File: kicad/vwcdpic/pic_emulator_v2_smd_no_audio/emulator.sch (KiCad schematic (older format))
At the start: 11 parts, among them P1 CONN_01X05, P2 CONN_01X02, U1 PIC12F629, U2 78L05

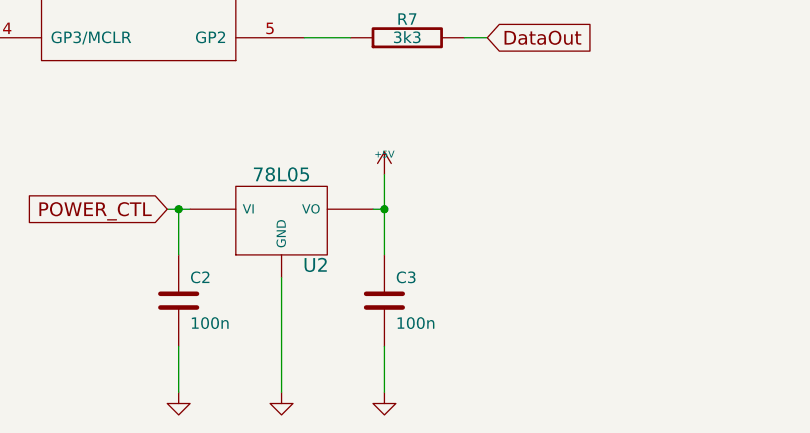
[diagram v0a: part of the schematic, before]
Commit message: update pcb with soic8 handsoldering module
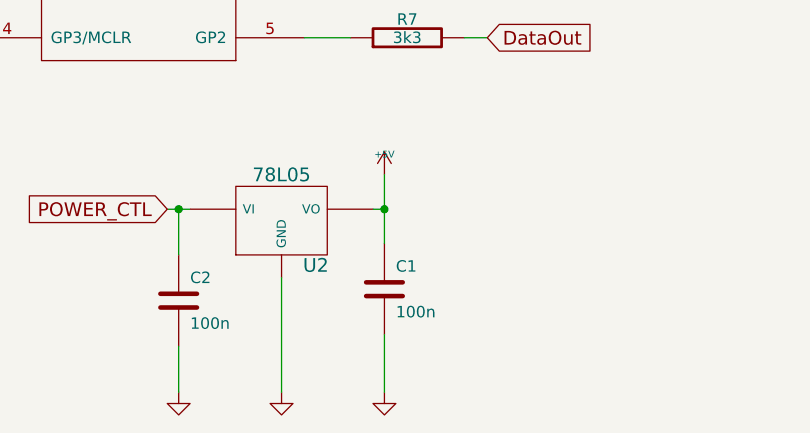
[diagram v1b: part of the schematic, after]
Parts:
- removed C3: 100n, symbol C
- added C1: 100n, symbol C
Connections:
- net +5V: now also C1.1
- net GND: now also C1.2
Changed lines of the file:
@@
 Wire Wire Line
 	5050 5050 5100 5050
-Connection ~ 5100 5050
 Wire Wire Line
 	8050 4000 8850 4000
@@
 	2200 4000 2300 4000
 Wire Wire Line
-	5100 5650 5100 5850
-Wire Wire Line
 	4200 5650 4200 5850
 Wire Wire Line
@@
 Wire Wire Line
 	4650 5350 4650 5850
-Wire Wire Line
-	5100 5250 5100 4900
 Wire Wire Line
 	4200 2850 4750 2850
@@
 $EndComp
 $Comp
-L GND #PWR07
-U 1 1 52D02F9D
-P 5100 5850
-F 0 "#PWR07" H 5100 5850 30  0001 C CNN
-F 1 "GND" H 5100 5780 30  0001 C CNN
-F 2 "" H 5100 5850 60  0001 C CNN
-F 3 "" H 5100 5850 60  0001 C CNN
-	1    5100 5850
-	1    0    0    -1
-$EndComp
-$Comp
-L C C3
-U 1 1 52D02F45
-P 5100 5450
-F 0 "C3" H 5150 5550 50  0000 L CNN
-F 1 "100n" H 5150 5350 50  0000 L CNN
-F 2 "" H 5100 5450 60  0001 C CNN
-F 3 "" H 5100 5450 60  0001 C CNN
-	1    5100 5450
-	1    0    0    -1
-$EndComp
-$Comp
 L C C2
 U 1 1 52D02F40
@@
 Wire Wire Line
 	4750 3800 4750 4000
+Wire Wire Line
+	5100 4900 5100 5200
+$Comp
+L C C1
+U 1 1 54325C4C
+P 5100 5400
+F 0 "C1" H 5150 5500 50  0000 L CNN
+F 1 "100n" H 5150 5300 50  0000 L CNN
+F 2 "" H 5100 5400 60  0001 C CNN
+F 3 "" H 5100 5400 60  0001 C CNN
+	1    5100 5400
+	1    0    0    -1
+$EndComp
+$Comp
+L GND #PWR07
+U 1 1 54325C93
+P 5100 5850
+F 0 "#PWR07" H 5100 5850 30  0001 C CNN
+F 1 "GND" H 5100 5780 30  0001 C CNN
+F 2 "" H 5100 5850 60  0001 C CNN
+F 3 "" H 5100 5850 60  0001 C CNN
+	1    5100 5850
+	1    0    0    -1
+$EndComp
+Wire Wire Line
+	5100 5600 5100 5850
+Connection ~ 5100 5050
 $EndSCHEMATC

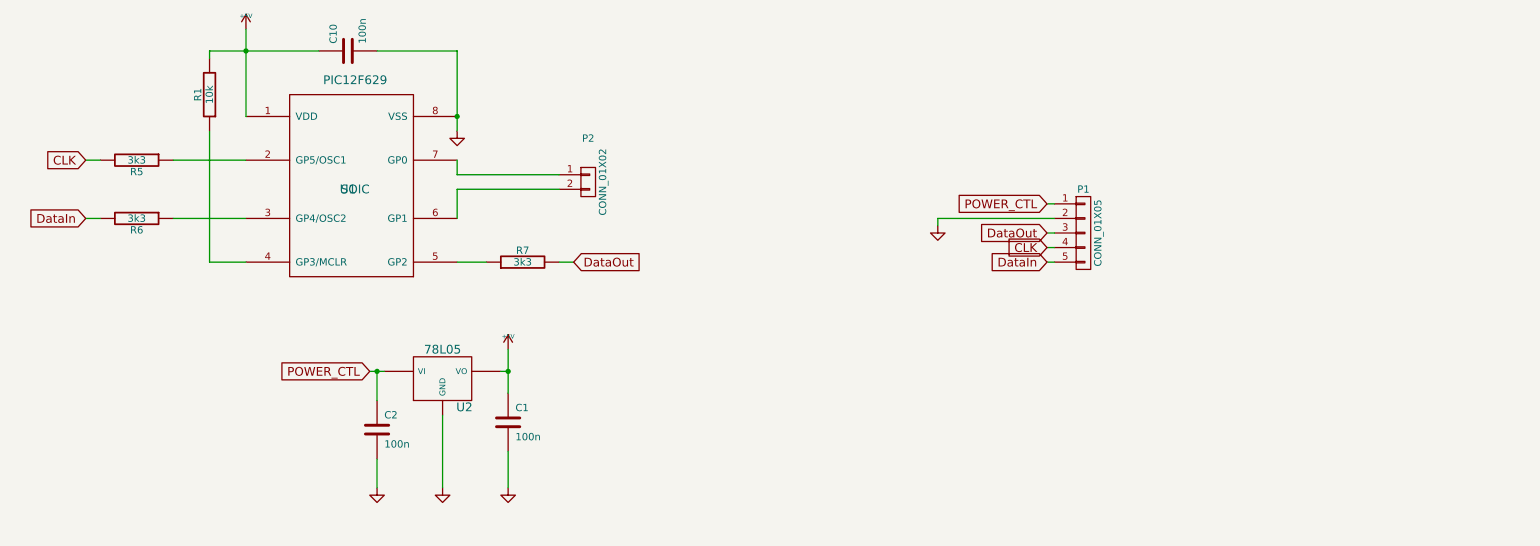
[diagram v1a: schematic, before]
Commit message: smd boards update: singleside smd, doubleside smd, minimized
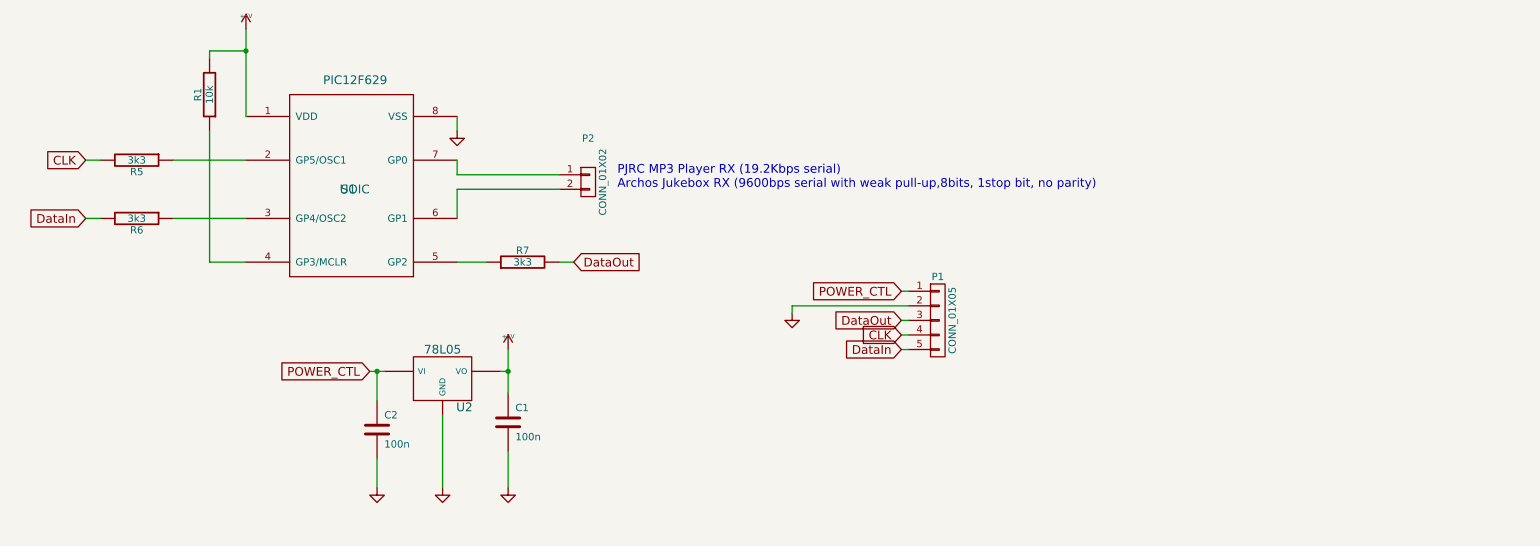
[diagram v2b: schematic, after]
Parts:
- removed C10: 100n, symbol C
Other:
- note added: "PJRC MP3 Player RX (19.2Kbps serial)\nArchos Jukebox RX (9600bps serial with weak pull-up,8bits, 1stop bit, no parity)\n"
- moved on the sheet: P1
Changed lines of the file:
@@
 	5050 5050 5100 5050
 Wire Wire Line
-	8050 4000 8850 4000
-Wire Wire Line
-	8800 4100 8850 4100
-Wire Wire Line
-	8800 4300 8850 4300
+	7050 4600 7850 4600
+Wire Wire Line
+	7800 4700 7850 4700
+Wire Wire Line
+	7800 4900 7850 4900
 Wire Wire Line
 	5550 4300 5450 4300
@@
 	2200 3600 2300 3600
 Wire Wire Line
-	8800 4200 8850 4200
-Wire Wire Line
-	8800 3900 8850 3900
+	7800 4800 7850 4800
+Wire Wire Line
+	7800 4500 7850 4500
 Wire Wire Line
 	4650 5350 4650 5850
-Wire Wire Line
-	4200 2850 4750 2850
-Wire Wire Line
-	4750 2850 4750 3400
-Connection ~ 4750 3300
 Wire Wire Line
 	4150 5050 4250 5050
 Text GLabel 4150 5050 0    60   Input ~ 0
 POWER_CTL
-$Comp
-L C C10
-U 1 1 52E79ABE
-P 4000 2850
-F 0 "C10" H 4050 2950 50  0000 L CNN
-F 1 "100n" H 4050 2750 50  0000 L CNN
-F 2 "" H 4000 2850 60  0001 C CNN
-F 3 "" H 4000 2850 60  0001 C CNN
-	1    4000 2850
-	0    -1   -1   0
-$EndComp
-Text GLabel 8800 3900 0    60   Input ~ 0
+Text GLabel 7800 4500 0    60   Input ~ 0
 POWER_CTL
 $Comp
 L GND #PWR01
 U 1 1 52D3D3F9
-P 8050 4050
-F 0 "#PWR01" H 8050 4050 30  0001 C CNN
-F 1 "GND" H 8050 3980 30  0001 C CNN
-F 2 "" H 8050 4050 60  0001 C CNN
-F 3 "" H 8050 4050 60  0001 C CNN
-	1    8050 4050
-	1    0    0    -1
-$EndComp
-Text GLabel 8800 4200 0    60   Input ~ 0
+P 7050 4650
+F 0 "#PWR01" H 7050 4650 30  0001 C CNN
+F 1 "GND" H 7050 4580 30  0001 C CNN
+F 2 "" H 7050 4650 60  0001 C CNN
+F 3 "" H 7050 4650 60  0001 C CNN
+	1    7050 4650
+	1    0    0    -1
+$EndComp
+Text GLabel 7800 4800 0    60   Input ~ 0
 CLK
-Text GLabel 8800 4300 0    60   Input ~ 0
+Text GLabel 7800 4900 0    60   Input ~ 0
 DataIn
-Text GLabel 8800 4100 0    60   Input ~ 0
+Text GLabel 7800 4700 0    60   Input ~ 0
 DataOut
 Text GLabel 5550 4300 2    60   Input ~ 0
@@
 L CONN_01X05 P1
 U 1 1 542D55A4
-P 9050 4100
-F 0 "P1" H 9050 4400 50  0000 C CNN
-F 1 "CONN_01X05" V 9150 4100 50  0000 C CNN
-F 2 "" H 9050 4100 60  0000 C CNN
-F 3 "" H 9050 4100 60  0000 C CNN
-	1    9050 4100
-	1    0    0    -1
-$EndComp
-Wire Wire Line
-	8050 4000 8050 4050
+P 8050 4700
+F 0 "P1" H 8050 5000 50  0000 C CNN
+F 1 "CONN_01X05" V 8150 4700 50  0000 C CNN
+F 2 "" H 8050 4700 60  0000 C CNN
+F 3 "" H 8050 4700 60  0000 C CNN
+	1    8050 4700
+	1    0    0    -1
+$EndComp
+Wire Wire Line
+	7050 4600 7050 4650
 $Comp
 L R R1
@@
 $EndComp
 Wire Wire Line
-	3050 2850 3800 2850
-Wire Wire Line
 	3300 2700 3300 3300
 Wire Wire Line
@@
 	5100 5600 5100 5850
 Connection ~ 5100 5050
+Wire Wire Line
+	3050 2850 3300 2850
+Wire Wire Line
+	4750 3300 4750 3400
+Text Notes 5850 3800 0    60   ~ 0
+PJRC MP3 Player RX (19.2Kbps serial)\nArchos Jukebox RX (9600bps serial with weak pull-up,8bits, 1stop bit, no parity)\n
 $EndSCHEMATC

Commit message: ICSP header added, serial header deleted, serial pins are on ICSP header
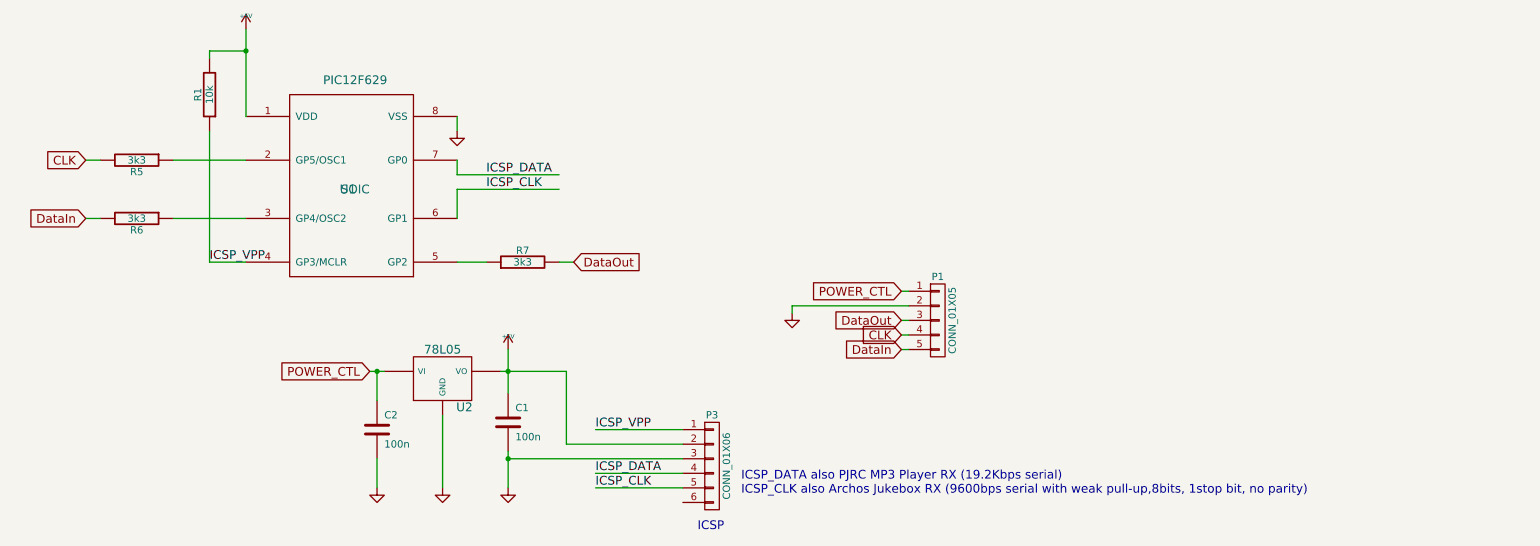
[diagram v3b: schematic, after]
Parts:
- removed P2: CONN_01X02, symbol CONN_01X02
- added P3: CONN_01X06, symbol CONN_01X06
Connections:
- net labels added: ICSP_CLK, ICSP_DATA, ICSP_VPP
- wire segments 29 -> 35
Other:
- note added: "ICSP"
- note added: "ICSP_DATA also PJRC MP3 Player RX (19.2Kbps serial)\nICSP_CLK also Archos Jukebox RX (9600bps serial with weak pull-up,8bits, 1stop bit, no parity)\n"
- note removed: "PJRC MP3 Player RX (19.2Kbps serial)\nArchos Jukebox RX (9600bps serial with weak pull-up,8bits, 1stop bit, no parity)\n"
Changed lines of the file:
@@
 Connection ~ 4200 5050
 Wire Wire Line
-	5050 5050 5100 5050
+	5050 5050 5500 5050
 Wire Wire Line
 	7050 4600 7850 4600
@@
 Wire Wire Line
 	3050 3400 3050 4300
-$Comp
-L CONN_01X02 P2
-U 1 1 542D83A2
-P 5650 3750
-F 0 "P2" H 5650 4050 50  0000 C CNN
-F 1 "CONN_01X02" V 5750 3750 50  0000 C CNN
-F 2 "" H 5650 3750 60  0000 C CNN
-F 3 "" H 5650 3750 60  0000 C CNN
-	1    5650 3750
-	1    0    0    -1
-$EndComp
 Wire Wire Line
 	3050 2900 3050 2850
@@
 Wire Wire Line
 	4750 3300 4750 3400
-Text Notes 5850 3800 0    60   ~ 0
-PJRC MP3 Player RX (19.2Kbps serial)\nArchos Jukebox RX (9600bps serial with weak pull-up,8bits, 1stop bit, no parity)\n
+Text Notes 6700 5900 0    60   ~ 0
+ICSP_DATA also PJRC MP3 Player RX (19.2Kbps serial)\nICSP_CLK also Archos Jukebox RX (9600bps serial with weak pull-up,8bits, 1stop bit, no parity)\n
+$Comp
+L CONN_01X06 P3
+U 1 1 54E5FBE4
+P 6500 5700
+F 0 "P3" H 6500 6050 50  0000 C CNN
+F 1 "CONN_01X06" V 6600 5700 50  0000 C CNN
+F 2 "" H 6500 5700 60  0000 C CNN
+F 3 "" H 6500 5700 60  0000 C CNN
+	1    6500 5700
+	1    0    0    -1
+$EndComp
+Text Notes 6400 6150 0    60   ~ 0
+ICSP
+Wire Wire Line
+	6300 5450 5700 5450
+Wire Wire Line
+	5500 5550 6300 5550
+Wire Wire Line
+	5100 5650 6300 5650
+Connection ~ 5100 5650
+Wire Wire Line
+	6300 5750 5700 5750
+Wire Wire Line
+	6300 5850 5700 5850
+Text Label 5700 5450 0    60   ~ 0
+ICSP_VPP
+Text Label 3050 4300 0    60   ~ 0
+ICSP_VPP
+Wire Wire Line
+	5500 5050 5500 5550
+Text Label 5700 5750 0    60   ~ 0
+ICSP_DATA
+Text Label 5700 5850 0    60   ~ 0
+ICSP_CLK
+Text Label 4950 3700 0    60   ~ 0
+ICSP_DATA
+Text Label 4950 3800 0    60   ~ 0
+ICSP_CLK
 $EndSCHEMATC

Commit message: updates
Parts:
- C1, C2: symbol C -> C-RESCUE-emulator
- R1, R5, R6, R7: symbol R -> R-RESCUE-emulator
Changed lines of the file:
@@
 EESchema Schematic File Version 2
+LIBS:emulator-rescue
 LIBS:power
 LIBS:device
@@
 LIBS:memory
 LIBS:xilinx
-LIBS:special
 LIBS:microcontrollers
 LIBS:dsp
@@
 $EndComp
 $Comp
-L C C2
+L C-RESCUE-emulator C2
 U 1 1 52D02F40
 P 4200 5450
@@
 $EndComp
 $Comp
-L R R7
+L R-RESCUE-emulator R7
 U 1 1 52D02B05
 P 5200 4300
@@
 $EndComp
 $Comp
-L R R5
+L R-RESCUE-emulator R5
 U 1 1 52D02AC2
 P 2550 3600
@@
 $EndComp
 $Comp
-L R R6
+L R-RESCUE-emulator R6
 U 1 1 52D02ABB
 P 2550 4000
@@
 	7050 4600 7050 4650
 $Comp
-L R R1
+L R-RESCUE-emulator R1
 U 1 1 52D03054
 P 3050 3150
@@
 	5100 4900 5100 5200
 $Comp
-L C C1
+L C-RESCUE-emulator C1
 U 1 1 54325C4C
 P 5100 5400
